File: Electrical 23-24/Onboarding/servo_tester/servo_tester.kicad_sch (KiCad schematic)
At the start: 18 parts, among them J1 Servo 1, J2 Servo 2, J3 Power In, J4 Prog, J5 Servo 3, SW1 RotaryEncoder_Switch, U1 ATtiny404-SS, U2 AP2205-33Y-13, U3 PCF8551ATT_AJ, U4 VIM-878-DP-FC-S-LV

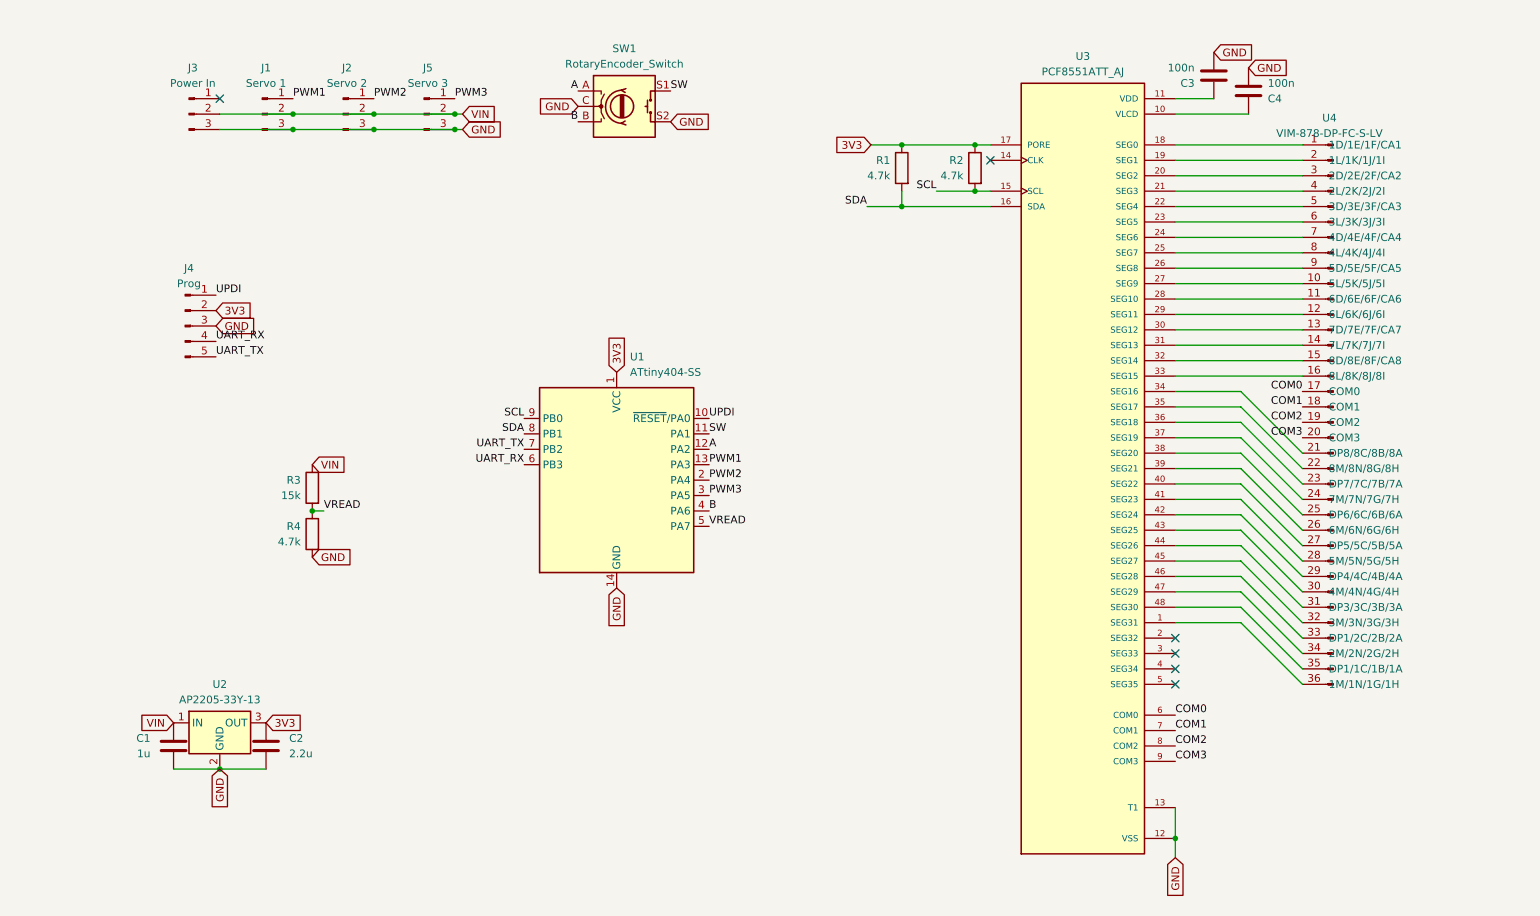
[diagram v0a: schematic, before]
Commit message: Add servo tester layout
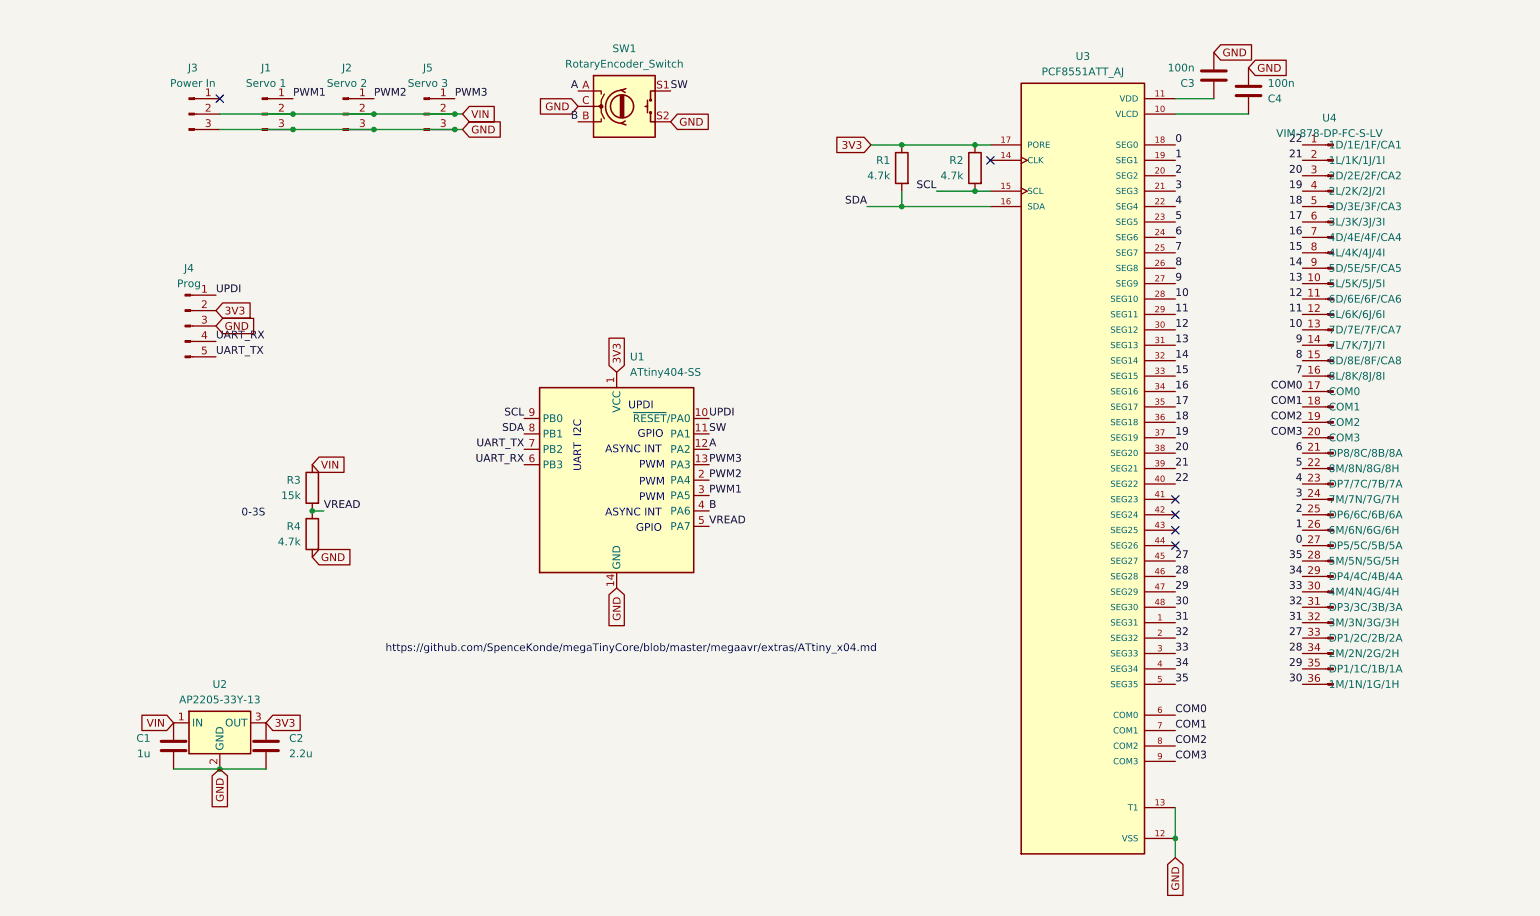
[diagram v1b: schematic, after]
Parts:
- C1, C2, C3, C4: footprint (none) -> Capacitor_SMD:C_0603_1608Metric_Pad1.08x0.95mm_HandSolder
- J1, J2, J3, J5: footprint (none) -> Connector_PinSocket_2.54mm:PinSocket_1x03_P2.54mm_Vertical
- J4: footprint (none) -> Connector_PinSocket_2.54mm:PinSocket_1x05_P2.54mm_Vertical
- R1, R2, R3, R4: footprint (none) -> Resistor_SMD:R_0603_1608Metric_Pad0.98x0.95mm_HandSolder
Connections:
- net PWM1: now also U1.3 (PA5); no longer U1.13 (PA3)
- net PWM3: now also U1.13 (PA3); no longer U1.3 (PA5)
- net 0: now reaches U3.18 (SEG0)
- net 0: now also U4.27 (DP5/5C/5B/5A); no longer U4.1 (1D/1E/1F/CA1)
- net 13: now reaches U4.10 (5L/5K/5J/5I)
- net 13: now also U3.31 (SEG13); no longer U3.27 (SEG9)
- net 10: now reaches U3.28 (SEG10)
- net 10: now also U4.13 (7D/7E/7F/CA7); no longer U4.11 (6D/6E/6F/CA6)
- net 11: now reaches U3.29 (SEG11), U4.12 (6L/6K/6J/6I)
- net 12: now reaches U3.30 (SEG12)
- net 12: now also U4.11 (6D/6E/6F/CA6); no longer U4.13 (7D/7E/7F/CA7)
- net 9: now reaches U4.14 (7L/7K/7J/7I)
- net 9: now also U3.27 (SEG9); no longer U3.31 (SEG13)
- net 14: now reaches U3.32 (SEG14)
- net 14: now also U4.9 (5D/5E/5F/CA5); no longer U4.15 (8D/8E/8F/CA8)
- net 15: now reaches U3.33 (SEG15)
- net 15: now also U4.8 (4L/4K/4J/4I); no longer U4.16 (8L/8K/8J/8I)
- net 1: now reaches U3.19 (SEG1)
- net 1: now also U4.26 (6M/6N/6G/6H); no longer U4.2 (1L/1K/1J/1I)
- net 16: now reaches U3.34 (SEG16)
- net 16: now also U4.7 (4D/4E/4F/CA4); no longer U4.21 (DP8/8C/8B/8A)
- net 17: now reaches U3.35 (SEG17)
- net 17: now also U4.6 (3L/3K/3J/3I); no longer U4.22 (8M/8N/8G/8H)
- net 18: now reaches U3.36 (SEG18)
- net 18: now also U4.5 (3D/3E/3F/CA3); no longer U4.23 (DP7/7C/7B/7A)
- net 19: now reaches U3.37 (SEG19)
- net 19: now also U4.4 (2L/2K/2J/2I); no longer U4.24 (7M/7N/7G/7H)
- net 2: now reaches U4.25 (DP6/6C/6B/6A)
- net 2: now also U3.20 (SEG2); no longer U3.38 (SEG20)
- net 21: now reaches U3.39 (SEG21)
- net 21: now also U4.2 (1L/1K/1J/1I); no longer U4.26 (6M/6N/6G/6H)
- net 22: now reaches U3.40 (SEG22)
- net 22: now also U4.1 (1D/1E/1F/CA1); no longer U4.27 (DP5/5C/5B/5A)
- net at U3.41 (SEG23): no longer U4.28 (5M/5N/5G/5H)
- net at U3.42 (SEG24): no longer U4.29 (DP4/4C/4B/4A)
- net 20: now reaches U4.3 (2D/2E/2F/CA2)
- net 20: now also U3.38 (SEG20); no longer U3.20 (SEG2)
- net at U3.43 (SEG25): no longer U4.30 (4M/4N/4G/4H)
- net at U3.44 (SEG26): no longer U4.31 (DP3/3C/3B/3A)
- net 27: now reaches U3.45 (SEG27)
- net 27: now also U4.33 (DP1/2C/2B/2A); no longer U4.32 (3M/3N/3G/3H)
- net 28: now reaches U3.46 (SEG28)
- net 28: now also U4.34 (2M/2N/2G/2H); no longer U4.33 (DP1/2C/2B/2A)
- net 29: now reaches U3.47 (SEG29)
- net 29: now also U4.35 (DP1/1C/1B/1A); no longer U4.34 (2M/2N/2G/2H)
- net 30: now reaches U3.48 (SEG30)
- net 30: now also U4.36 (1M/1N/1G/1H); no longer U4.35 (DP1/1C/1B/1A)
- net 31: now reaches U3.1 (SEG31)
- net 31: now also U4.32 (3M/3N/3G/3H); no longer U4.36 (1M/1N/1G/1H)
- net 3: now reaches U3.21 (SEG3)
- net 3: now also U4.24 (7M/7N/7G/7H); no longer U4.4 (2L/2K/2J/2I)
- net 4: now reaches U3.22 (SEG4)
- net 4: now also U4.23 (DP7/7C/7B/7A); no longer U4.5 (3D/3E/3F/CA3)
- net 5: now reaches U3.23 (SEG5)
- net 5: now also U4.22 (8M/8N/8G/8H); no longer U4.6 (3L/3K/3J/3I)
- net 6: now reaches U3.24 (SEG6)
- net 6: now also U4.21 (DP8/8C/8B/8A); no longer U4.7 (4D/4E/4F/CA4)
- net 7: now reaches U3.25 (SEG7)
- net 7: now also U4.16 (8L/8K/8J/8I); no longer U4.8 (4L/4K/4J/4I)
- net 8: now reaches U3.26 (SEG8)
- net 8: now also U4.15 (8D/8E/8F/CA8); no longer U4.9 (5D/5E/5F/CA5)
- net 32: now reaches U3.2 (SEG32)
- net 32: now also U4.31 (DP3/3C/3B/3A)
- net 33: now reaches U3.3 (SEG33)
- net 33: now also U4.30 (4M/4N/4G/4H)
- net 34: now reaches U3.4 (SEG34)
- net 34: now also U4.29 (DP4/4C/4B/4A)
- net 35: now reaches U3.5 (SEG35)
- net 35: now also U4.28 (5M/5N/5G/5H)
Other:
- note added: "0-3S"
- note added: "ASYNC INT"
- note added: "GPIO"
- note added: "I2C"
- note added: "PWM"
- note added: "UART"
- note added: "UPDI"
- note added: "https://github.com/SpenceKonde/megaTinyCore/blob/master/megaavr/extras/ATtiny_x04.md"

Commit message: Updated folders and schematic for onboarding
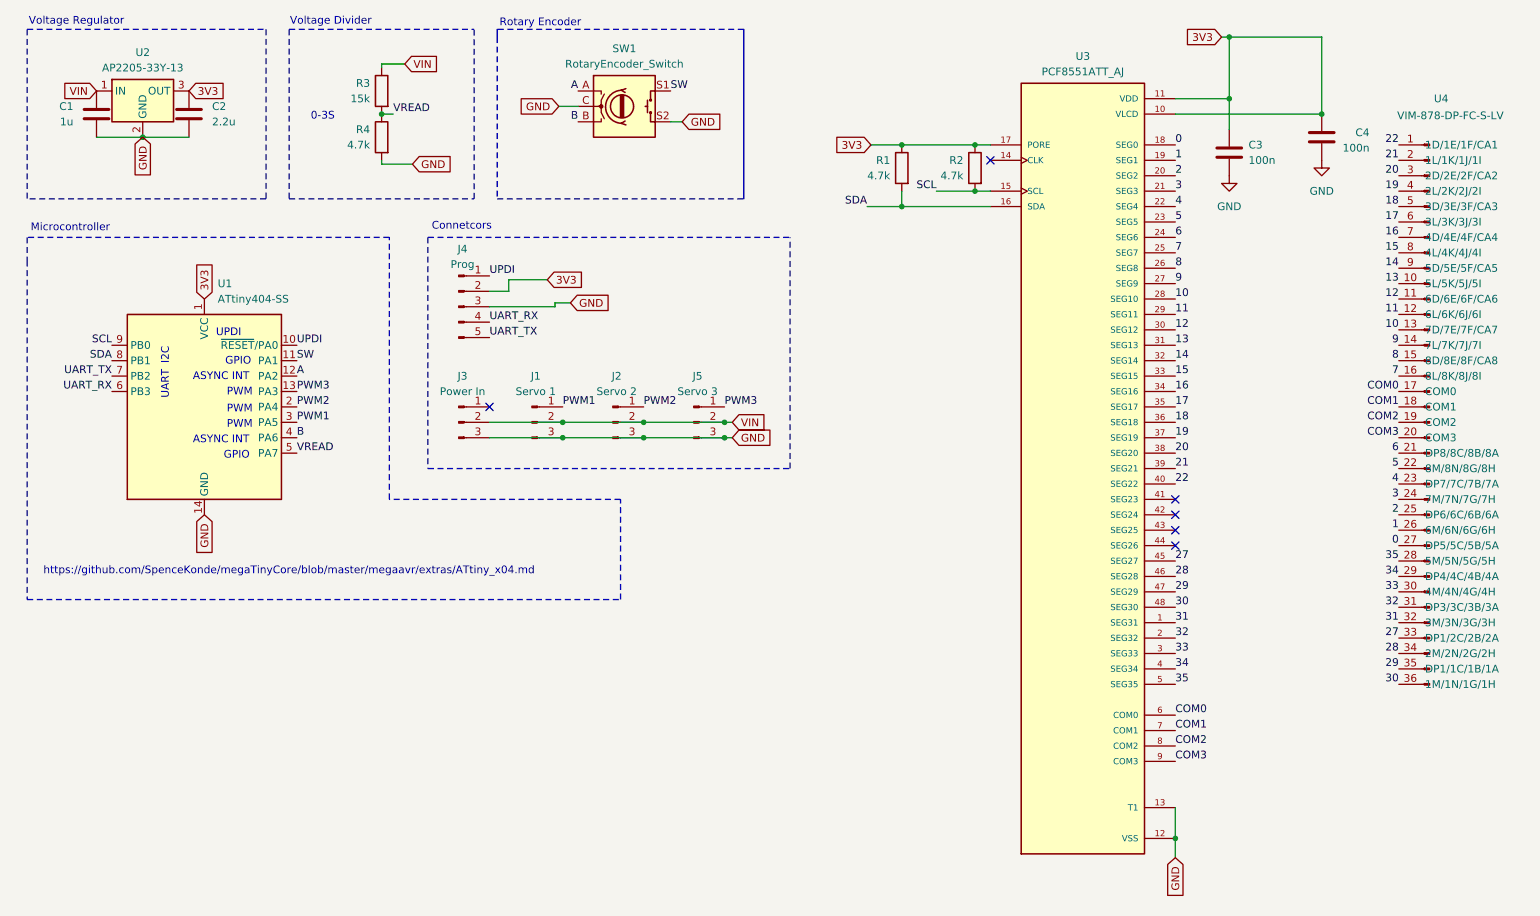
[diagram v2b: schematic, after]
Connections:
- net 3V3: now also C3.1, C4.1, U3.10 (VLCD), U3.11 (VDD)
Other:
- note added: "Connetcors"
- note added: "Microcontroller"
- note added: "Rotary Encoder"
- note added: "Voltage Divider"
- note added: "Voltage Regulator"
- moved on the sheet: C1, C2, C3, C4, J1, J2, J3, J4, J5, R3, R4, U1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
